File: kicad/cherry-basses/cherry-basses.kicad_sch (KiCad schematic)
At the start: 36 parts, among them SW1.1 SPST, SW1.2 SPST, SW1.3 SPST, SW1.4 SPST, SW1.5 SPST, SW1.6 SPST, SW1.7 SPST, SW1.8 SPST, SW2.0 SPST, SW2.1 SPST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

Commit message: cherry basses: replace components for rendering, add some vias
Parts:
- Conn1: footprint Connector_Multicomp:Multicomp_MC9A12-2634_2x13_P2.54mm_Vertical -> Connector_IDC:IDC-Header_2x13_P2.54mm_Vertical
- R1, R2: footprint Resistor_SMD:R_1206_3216Metric_Pad1.42x1.75mm_HandSolder -> Resistor_SMD:R_1206_3216Metric_Pad1.30x1.75mm_HandSolder
- SW.PushPull.1: footprint Library:Neltron-5523S-XX-10-X-Terminal-P5.0mm-7.5x10 -> Connector_Molex:Molex_KK-254_AE-6410-02A_1x02_P2.54mm_Vertical
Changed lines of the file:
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@@
     (property "Reference" "Conn1" (id 0) (at 191.77 18.6182 0))
     (property "Value" "Conn_02x13_Odd_Even" (id 1) (at 191.77 20.9296 0))
-    (property "Footprint" "Connector_Multicomp:Multicomp_MC9A12-2634_2x13_P2.54mm_Vertical" (id 2) (at 190.5 39.37 0)
+    (property "Footprint" "Connector_IDC:IDC-Header_2x13_P2.54mm_Vertical" (id 2) (at 190.5 39.37 0)
       (effects (font (size 1.27 1.27)) hide)
     )
@@
       (effects (font (size 1.27 1.27)) (justify left))
     )
-    (property "Footprint" "Resistor_SMD:R_1206_3216Metric_Pad1.42x1.75mm_HandSolder" (id 2) (at 31.242 50.8 90)
+    (property "Footprint" "Resistor_SMD:R_1206_3216Metric_Pad1.30x1.75mm_HandSolder" (id 2) (at 31.242 50.8 90)
       (effects (font (size 1.27 1.27)) hide)
     )
@@
       (effects (font (size 1.27 1.27)) (justify left))
     )
-    (property "Footprint" "Resistor_SMD:R_1206_3216Metric_Pad1.42x1.75mm_HandSolder" (id 2) (at 31.242 80.01 90)
+    (property "Footprint" "Resistor_SMD:R_1206_3216Metric_Pad1.30x1.75mm_HandSolder" (id 2) (at 31.242 80.01 90)
       (effects (font (size 1.27 1.27)) hide)
     )
@@
     (property "Reference" "SW.PushPull.1" (id 0) (at 160.02 28.321 0))
     (property "Value" "SPST" (id 1) (at 160.02 30.6324 0))
-    (property "Footprint" "Library:Neltron-5523S-XX-10-X-Terminal-P5.0mm-7.5x10" (id 2) (at 160.02 34.29 0)
+    (property "Footprint" "Connector_Molex:Molex_KK-254_AE-6410-02A_1x02_P2.54mm_Vertical" (id 2) (at 160.02 34.29 0)
       (effects (font (size 1.27 1.27)) hide)
     )
@@
     )
     (path "/00000000-0000-0000-0000-00005da5dbd2"
-      (reference "Conn1") (unit 1) (value "Conn_02x13_Odd_Even") (footprint "Connector_Multicomp:Multicomp_MC9A12-2634_2x13_P2.54mm_Vertical")
+      (reference "Conn1") (unit 1) (value "Conn_02x13_Odd_Even") (footprint "Connector_IDC:IDC-Header_2x13_P2.54mm_Vertical")
     )
     (path "/00000000-0000-0000-0000-00005afca3f5"
@@
     )
     (path "/00000000-0000-0000-0000-00005dae40ba"
-      (reference "R1") (unit 1) (value "10k") (footprint "Resistor_SMD:R_1206_3216Metric_Pad1.42x1.75mm_HandSolder")
+      (reference "R1") (unit 1) (value "10k") (footprint "Resistor_SMD:R_1206_3216Metric_Pad1.30x1.75mm_HandSolder")
     )
     (path "/00000000-0000-0000-0000-00005dae47d3"
-      (reference "R2") (unit 1) (value "10k") (footprint "Resistor_SMD:R_1206_3216Metric_Pad1.42x1.75mm_HandSolder")
+      (reference "R2") (unit 1) (value "10k") (footprint "Resistor_SMD:R_1206_3216Metric_Pad1.30x1.75mm_HandSolder")
     )
     (path "/bac3a122-34cf-4c7a-82bb-1b2dfbc8b2e7"
-      (reference "SW.PushPull.1") (unit 1) (value "SPST") (footprint "Library:Neltron-5523S-XX-10-X-Terminal-P5.0mm-7.5x10")
+      (reference "SW.PushPull.1") (unit 1) (value "SPST") (footprint "Connector_Molex:Molex_KK-254_AE-6410-02A_1x02_P2.54mm_Vertical")
     )
     (path "/00000000-0000-0000-0000-00005afc9c1d"

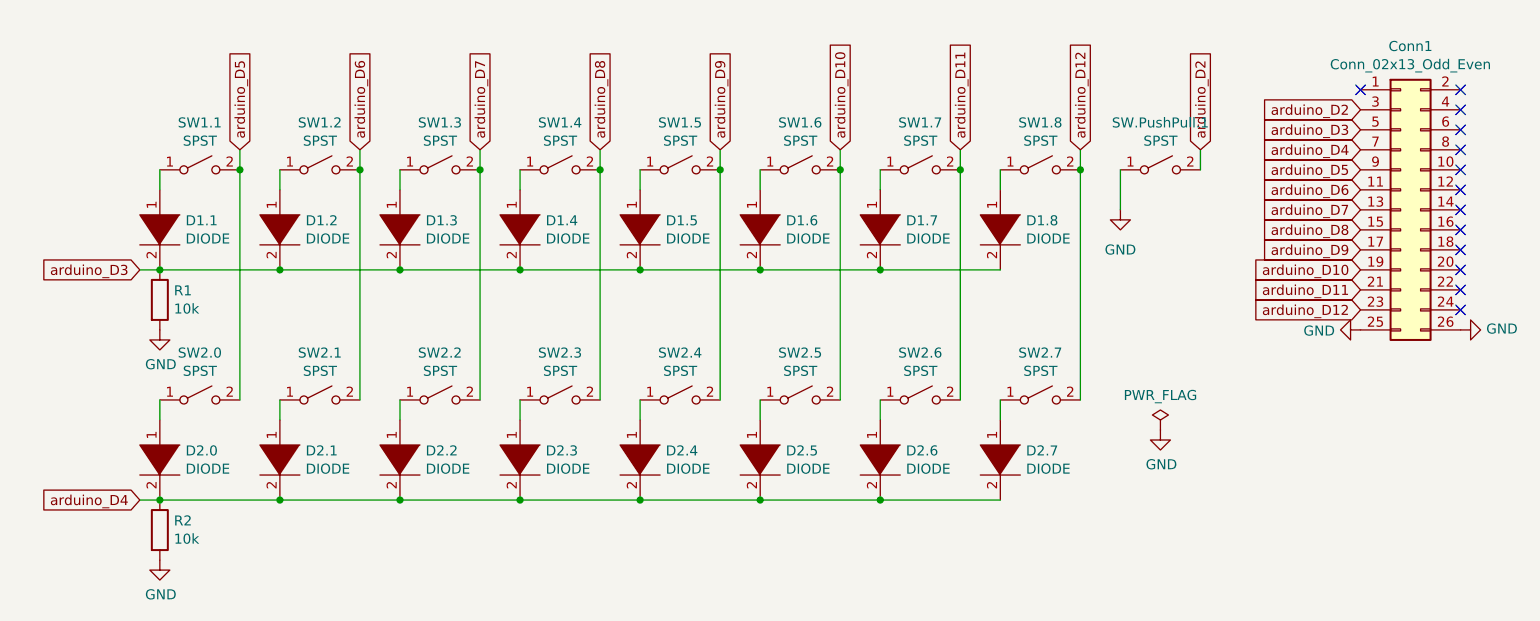
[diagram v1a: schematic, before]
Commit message: Replace pspice diodes with proper schottky diodes on cherry basses schematics
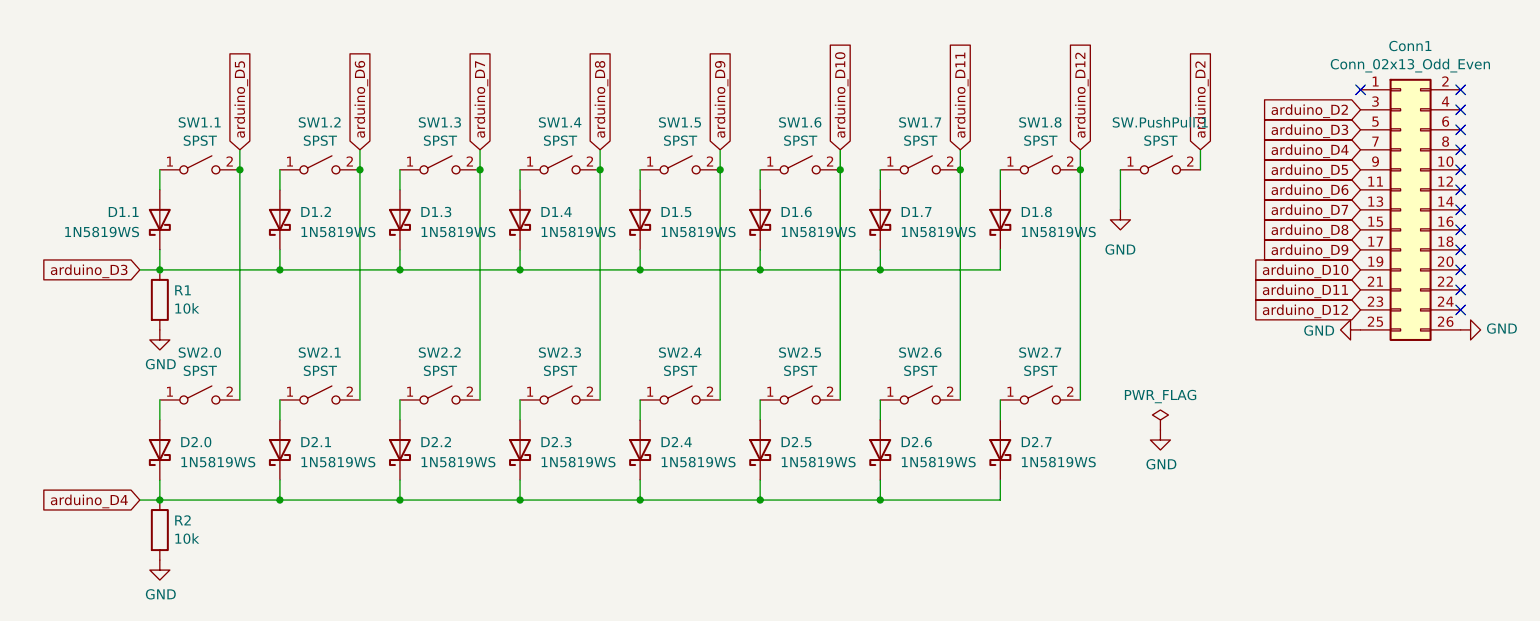
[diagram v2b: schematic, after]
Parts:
- Conn1: LCSC Part # (none) -> C692426
- D1.1, D1.2, D1.3, D1.4, D1.5, D1.6, D1.7, D1.8, D2.0, D2.1, D2.2, D2.3, D2.4, D2.5, D2.6, D2.7: value DIODE -> 1N5819WS; symbol pspice:DIODE -> Diode:1N5819WS; LCSC Part # (none) -> C191023
- R1, R2: LCSC Part # (none) -> C17902
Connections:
- net arduino_D3: now also D1.1.1 (K), D1.2.1 (K), D1.3.1 (K), D1.4.1 (K), D1.5.1 (K), D1.6.1 (K), D1.7.1 (K), D1.8.1 (K); no longer D1.1.2 (A), D1.2.2 (A), D1.3.2 (A), D1.4.2 (A), D1.5.2 (A), D1.6.2 (A), D1.7.2 (A), D1.8.2 (A)
- net arduino_D4: now also D2.0.1 (K), D2.1.1 (K), D2.2.1 (K), D2.3.1 (K), D2.4.1 (K), D2.5.1 (K), D2.6.1 (K), D2.7.1 (K); no longer D2.0.2 (A), D2.1.2 (A), D2.2.2 (A), D2.3.2 (A), D2.4.2 (A), D2.5.2 (A), D2.6.2 (A), D2.7.2 (A)
- net at SW1.1.1 (A): now also D1.1.2 (A); no longer D1.1.1 (K)
- net at SW1.2.1 (A): now also D1.2.2 (A); no longer D1.2.1 (K)
- net at SW2.1.1 (A): now also D2.1.2 (A); no longer D2.1.1 (K)
- net at SW2.2.1 (A): now also D2.2.2 (A); no longer D2.2.1 (K)
- net at SW1.3.1 (A): now also D1.3.2 (A); no longer D1.3.1 (K)
- net at SW1.4.1 (A): now also D1.4.2 (A); no longer D1.4.1 (K)
- net at SW2.3.1 (A): now also D2.3.2 (A); no longer D2.3.1 (K)
- net at SW2.4.1 (A): now also D2.4.2 (A); no longer D2.4.1 (K)
- net at SW1.5.1 (A): now also D1.5.2 (A); no longer D1.5.1 (K)
- net at SW1.6.1 (A): now also D1.6.2 (A); no longer D1.6.1 (K)
- net at SW2.5.1 (A): now also D2.5.2 (A); no longer D2.5.1 (K)
- net at SW2.0.1 (A): now also D2.0.2 (A); no longer D2.0.1 (K)
- net at SW1.7.1 (A): now also D1.7.2 (A); no longer D1.7.1 (K)
- net at SW2.6.1 (A): now also D2.6.2 (A); no longer D2.6.1 (K)
- net at SW1.8.1 (A): now also D1.8.2 (A); no longer D1.8.1 (K)
- net at SW2.7.1 (A): now also D2.7.2 (A); no longer D2.7.1 (K)
